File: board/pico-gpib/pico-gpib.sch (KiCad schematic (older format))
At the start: 37 parts, among them J2 USB_B_Micro, J3 RasPi_Header_40W, J4 Debug, U1 RP2040, U4 W25Q128JVS, U5 NCP1117-3.3, U6 CAT24C32, Y1 12M10PI/XT324-10/20

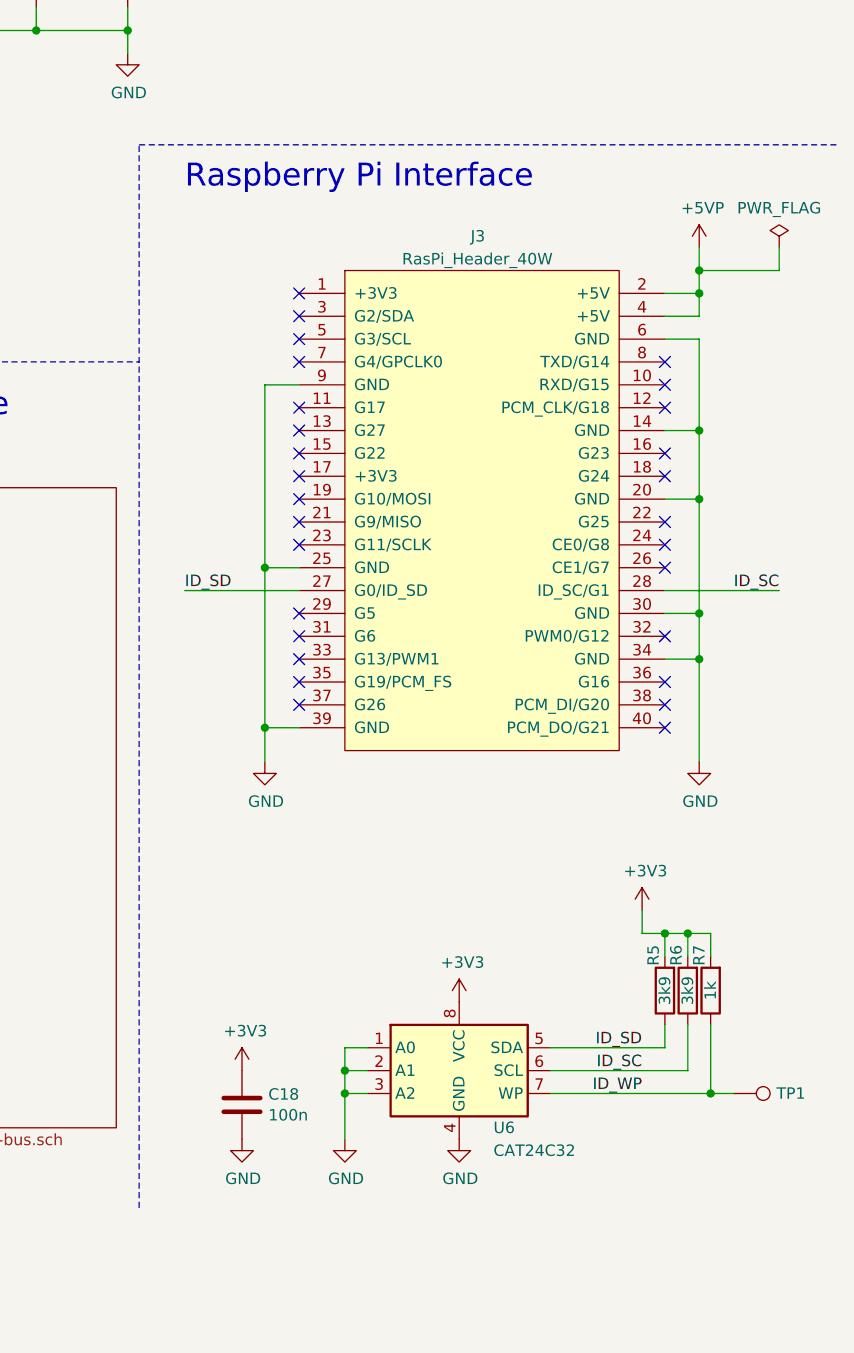
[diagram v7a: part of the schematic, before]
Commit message: Move ID EEPROM to RPI 3V3 supply.
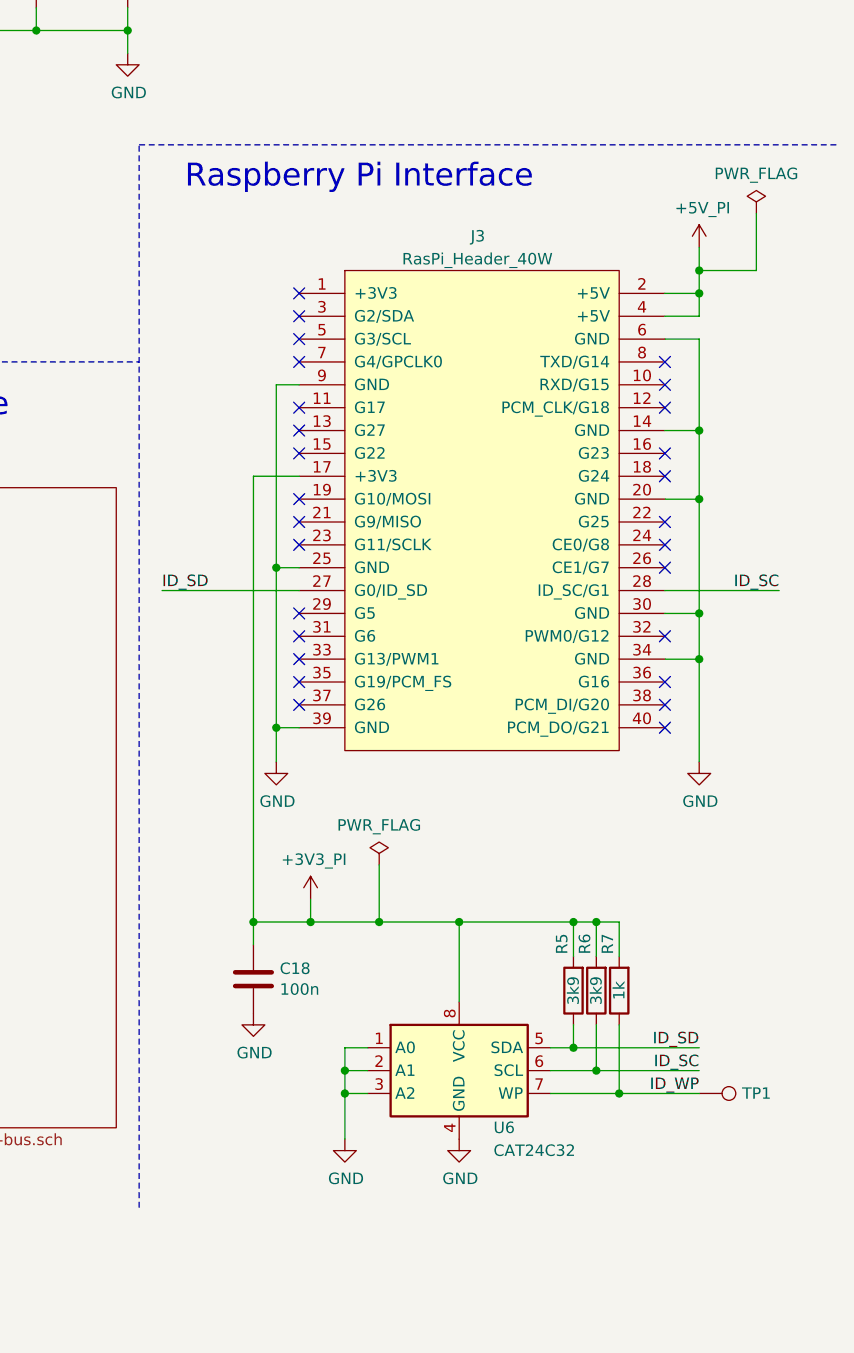
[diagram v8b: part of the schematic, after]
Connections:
- net +3V3: no longer C18.1, R5.2, R6.2, R7.2, U6.8 (VCC)
- net +3V3_PI: now reaches J3.17 (+3V3)
- net +3V3_PI: now also C18.1, R5.2, R6.2, R7.2, U6.8 (VCC)
- net +5VP renamed +5V_PI
- no-connect marks 40 -> 39
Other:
- moved on the sheet: C18, R5, R6, R7, TP1
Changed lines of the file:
@@
-$EndComp
-$Comp
-L power:+3V3 #PWR013
-U 1 1 63111360
-P 9550 5600
-F 0 "#PWR013" H 9550 5450 50  0001 C CNN
-F 1 "+3V3" H 9565 5773 50  0000 C CNN
-F 2 "" H 9550 5600 50  0001 C CNN
-F 3 "" H 9550 5600 50  0001 C CNN
-	1    9550 5600
-	1    0    0    -1
 $EndComp
 $Comp
@@
 Wire Wire Line
 	9050 6000 9050 6200
-Text Label 10350 5800 2    50   ~ 0
+Text Label 10600 5800 2    50   ~ 0
 ID_SD
-Text Label 10350 5900 2    50   ~ 0
+Text Label 10600 5900 2    50   ~ 0
 ID_SC
-Text Label 10350 6000 2    50   ~ 0
+Text Label 10600 6000 2    50   ~ 0
 ID_WP
 $Comp
 L Device:R R5
 U 1 1 63178FFC
-P 10450 5550
-F 0 "R5" V 10500 5350 50  0000 L CNN
-F 1 "3k9" V 10450 5550 50  0000 C CNN
-F 2 "Resistor_SMD:R_0402_1005Metric" V 10380 5550 50  0001 C CNN
-F 3 "~" H 10450 5550 50  0001 C CNN
-	1    10450 5550
+P 10050 5550
+F 0 "R5" V 10100 5300 50  0000 L CNN
+F 1 "3k9" V 10050 5550 50  0000 C CNN
+F 2 "Resistor_SMD:R_0402_1005Metric" V 9980 5550 50  0001 C CNN
+F 3 "~" H 10050 5550 50  0001 C CNN
+	1    10050 5550
 	-1   0    0    1
 $EndComp
@@
 L Device:R R6
 U 1 1 6317A37B
-P 10550 5550
-F 0 "R6" V 10600 5350 50  0000 L CNN
-F 1 "3k9" V 10550 5550 50  0000 C CNN
-F 2 "Resistor_SMD:R_0402_1005Metric" V 10480 5550 50  0001 C CNN
-F 3 "~" H 10550 5550 50  0001 C CNN
-	1    10550 5550
+P 10150 5550
+F 0 "R6" V 10200 5300 50  0000 L CNN
+F 1 "3k9" V 10150 5550 50  0000 C CNN
+F 2 "Resistor_SMD:R_0402_1005Metric" V 10080 5550 50  0001 C CNN
+F 3 "~" H 10150 5550 50  0001 C CNN
+	1    10150 5550
 	-1   0    0    1
 $EndComp
@@
 L Device:R R7
 U 1 1 6317ACAC
-P 10650 5550
-F 0 "R7" V 10700 5350 50  0000 L CNN
-F 1 "1k" V 10650 5550 50  0000 C CNN
-F 2 "Resistor_SMD:R_0402_1005Metric" V 10580 5550 50  0001 C CNN
-F 3 "~" H 10650 5550 50  0001 C CNN
-	1    10650 5550
+P 10250 5550
+F 0 "R7" V 10300 5300 50  0000 L CNN
+F 1 "1k" V 10250 5550 50  0000 C CNN
+F 2 "Resistor_SMD:R_0402_1005Metric" V 10180 5550 50  0001 C CNN
+F 3 "~" H 10250 5550 50  0001 C CNN
+	1    10250 5550
 	-1   0    0    1
 $EndComp
 Wire Wire Line
-	10450 5800 10450 5700
-Wire Wire Line
-	9950 5800 10450 5800
-Wire Wire Line
-	10550 5900 10550 5700
-Wire Wire Line
-	9950 5900 10550 5900
-Wire Wire Line
-	10650 6000 10650 5700
-Wire Wire Line
-	9950 6000 10650 6000
-Wire Wire Line
-	10650 6000 10750 6000
-Connection ~ 10650 6000
+	10050 5800 10050 5700
+Wire Wire Line
+	9950 5800 10050 5800
+Wire Wire Line
+	10150 5900 10150 5700
+Wire Wire Line
+	9950 5900 10150 5900
+Wire Wire Line
+	10250 6000 10250 5700
+Wire Wire Line
+	9950 6000 10250 6000
 $Comp
 L Connector:TestPoint TP1
 U 1 1 631B8D19
-P 10750 6000
-F 0 "TP1" V 10750 6188 50  0000 L CNN
-F 1 "TestPoint" V 10795 6188 50  0001 L CNN
-F 2 "TestPoint:TestPoint_Pad_D1.0mm" H 10950 6000 50  0001 C CNN
-F 3 "~" H 10950 6000 50  0001 C CNN
-	1    10750 6000
+P 10600 6000
+F 0 "TP1" V 10600 6188 50  0000 L CNN
+F 1 "TestPoint" V 10645 6188 50  0001 L CNN
+F 2 "TestPoint:TestPoint_Pad_D1.0mm" H 10800 6000 50  0001 C CNN
+F 3 "~" H 10800 6000 50  0001 C CNN
+	1    10600 6000
 	0    1    1    0
 $EndComp
-$Comp
-L power:+3V3 #PWR015
-U 1 1 631B93BC
-P 10350 5200
-F 0 "#PWR015" H 10350 5050 50  0001 C CNN
-F 1 "+3V3" H 10365 5373 50  0000 C CNN
-F 2 "" H 10350 5200 50  0001 C CNN
-F 3 "" H 10350 5200 50  0001 C CNN
-	1    10350 5200
-	1    0    0    -1
-$EndComp
-Wire Wire Line
-	10350 5200 10350 5300
-Wire Wire Line
-	10350 5300 10450 5300
-Wire Wire Line
-	10650 5300 10650 5400
-Wire Wire Line
-	10550 5400 10550 5300
-Connection ~ 10550 5300
-Wire Wire Line
-	10550 5300 10650 5300
-Wire Wire Line
-	10450 5400 10450 5300
-Connection ~ 10450 5300
-Wire Wire Line
-	10450 5300 10550 5300
+Wire Wire Line
+	10250 5250 10250 5400
+Wire Wire Line
+	10150 5400 10150 5250
+Connection ~ 10150 5250
+Wire Wire Line
+	10150 5250 10250 5250
+Wire Wire Line
+	10050 5400 10050 5250
+Connection ~ 10050 5250
+Wire Wire Line
+	10050 5250 10150 5250
 NoConn ~ 8850 2600
 NoConn ~ 8850 2700
@@
 NoConn ~ 8850 3100
 NoConn ~ 8850 3200
-NoConn ~ 8850 3300
 NoConn ~ 8850 3400
 NoConn ~ 8850 3500
@@
 L power:GND #PWR017
 U 1 1 63499121
-P 8600 6200
-F 0 "#PWR017" H 8600 5950 50  0001 C CNN
-F 1 "GND" H 8605 6027 50  0000 C CNN
-F 2 "" H 8600 6200 50  0001 C CNN
-F 3 "" H 8600 6200 50  0001 C CNN
-	1    8600 6200
-	1    0    0    -1
-$EndComp
-$Comp
-L power:+3V3 #PWR016
-U 1 1 634996AF
-P 8600 5900
-F 0 "#PWR016" H 8600 5750 50  0001 C CNN
-F 1 "+3V3" H 8615 6073 50  0000 C CNN
-F 2 "" H 8600 5900 50  0001 C CNN
-F 3 "" H 8600 5900 50  0001 C CNN
-	1    8600 5900
+P 8650 5650
+F 0 "#PWR017" H 8650 5400 50  0001 C CNN
+F 1 "GND" H 8655 5477 50  0000 C CNN
+F 2 "" H 8650 5650 50  0001 C CNN
+F 3 "" H 8650 5650 50  0001 C CNN
+	1    8650 5650
 	1    0    0    -1
 $EndComp
@@
 L Device:C C18
 U 1 1 634996B9
-P 8600 6050
-F 0 "C18" H 8715 6096 50  0000 L CNN
-F 1 "100n" H 8715 6005 50  0000 L CNN
-F 2 "Capacitor_SMD:C_0402_1005Metric" H 8638 5900 50  0001 C CNN
-F 3 "~" H 8600 6050 50  0001 C CNN
-	1    8600 6050
+P 8650 5500
+F 0 "C18" H 8765 5546 50  0000 L CNN
+F 1 "100n" H 8765 5455 50  0000 L CNN
+F 2 "Capacitor_SMD:C_0402_1005Metric" H 8688 5350 50  0001 C CNN
+F 3 "~" H 8650 5500 50  0001 C CNN
+	1    8650 5500
 	1    0    0    -1
 $EndComp
@@
 Connection ~ 10600 3400
 Wire Wire Line
-	8850 2900 8700 2900
+	8850 2900 8750 2900
 NoConn ~ 10450 4400
 NoConn ~ 10450 4300
@@
 Text Label 10950 3800 2    50   ~ 0
 ID_SC
-Text Label 8350 3800 0    50   ~ 0
+Text Label 8250 3800 0    50   ~ 0
 ID_SD
 Wire Wire Line
 	10450 3800 10950 3800
 Wire Wire Line
-	8850 3800 8350 3800
+	8850 3800 8250 3800
 $Comp
 L power:GND #PWR0108
 U 1 1 61F681DC
-P 8700 4550
-F 0 "#PWR0108" H 8700 4300 50  0001 C CNN
-F 1 "GND" H 8705 4377 50  0000 C CNN
-F 2 "" H 8700 4550 50  0001 C CNN
-F 3 "" H 8700 4550 50  0001 C CNN
-	1    8700 4550
+P 8750 4550
+F 0 "#PWR0108" H 8750 4300 50  0001 C CNN
+F 1 "GND" H 8755 4377 50  0000 C CNN
+F 2 "" H 8750 4550 50  0001 C CNN
+F 3 "" H 8750 4550 50  0001 C CNN
+	1    8750 4550
 	1    0    0    -1
 $EndComp
@@
 $EndComp
 Wire Wire Line
-	8700 4400 8700 4550
-Connection ~ 8700 4400
-Wire Wire Line
-	8850 4400 8700 4400
-Wire Wire Line
-	8700 3700 8700 4400
-Connection ~ 8700 3700
-Wire Wire Line
-	8850 3700 8700 3700
-Wire Wire Line
-	8700 2900 8700 3700
+	8750 4400 8750 4550
+Connection ~ 8750 4400
+Wire Wire Line
+	8850 4400 8750 4400
+Wire Wire Line
+	8750 3700 8750 4400
+Connection ~ 8750 3700
+Wire Wire Line
+	8850 3700 8750 3700
+Wire Wire Line
+	8750 2900 8750 3700
 Wire Wire Line
 	10600 4100 10600 4550
@@
 Wire Notes Line
 	8150 1850 11200 1850
-$Comp
-L power:+5VP #PWR0131
-U 1 1 620A68D2
+Connection ~ 10600 2500
+$Comp
+L power:PWR_FLAG #FLG0103
+U 1 1 626F016E
+P 10850 2150
+F 0 "#FLG0103" H 10850 2225 50  0001 C CNN
+F 1 "PWR_FLAG" H 10850 2323 50  0000 C CNN
+F 2 "" H 10850 2150 50  0001 C CNN
+F 3 "~" H 10850 2150 50  0001 C CNN
+	1    10850 2150
+	1    0    0    -1
+$EndComp
+Connection ~ 10050 5800
+Connection ~ 10150 5900
+Wire Wire Line
+	10050 5800 10600 5800
+Wire Wire Line
+	10150 5900 10600 5900
+Wire Wire Line
+	10250 6000 10600 6000
+Connection ~ 10250 6000
+Wire Wire Line
+	8850 3300 8650 3300
+Wire Wire Line
+	8650 3300 8650 5250
+Wire Wire Line
+	8650 5250 8900 5250
+Wire Wire Line
+	8650 5350 8650 5250
+Connection ~ 8650 5250
+Wire Wire Line
+	9550 5600 9550 5250
+Connection ~ 9550 5250
+Wire Wire Line
+	9550 5250 10050 5250
+$Comp
+L local:+5V_PI #PWR0131
+U 1 1 6281E388
 P 10600 2300
 F 0 "#PWR0131" H 10600 2150 50  0001 C CNN
-F 1 "+5VP" H 10615 2473 50  0000 C CNN
+F 1 "+5V_PI" H 10615 2473 50  0000 C CNN
 F 2 "" H 10600 2300 50  0001 C CNN
 F 3 "" H 10600 2300 50  0001 C CNN
@@
 	1    0    0    -1
 $EndComp
-Connection ~ 10600 2500
 Wire Wire Line
 	10600 2300 10600 2400
-$Comp
-L power:PWR_FLAG #FLG0103
-U 1 1 626F016E
-P 10950 2300
-F 0 "#FLG0103" H 10950 2375 50  0001 C CNN
-F 1 "PWR_FLAG" H 10950 2473 50  0000 C CNN
-F 2 "" H 10950 2300 50  0001 C CNN
-F 3 "~" H 10950 2300 50  0001 C CNN
-	1    10950 2300
-	1    0    0    -1
-$EndComp
-Wire Wire Line
-	10950 2300 10950 2400
-Wire Wire Line
-	10950 2400 10600 2400
+Wire Wire Line
+	10600 2400 10850 2400
+Wire Wire Line
+	10850 2400 10850 2150
 Connection ~ 10600 2400
 Wire Wire Line
 	10600 2400 10600 2500
+$Comp
+L local:+3V3_PI #PWR0132
+U 1 1 62830914
+P 8900 5150
+F 0 "#PWR0132" H 8900 5000 50  0001 C CNN
+F 1 "+3V3_PI" H 8915 5323 50  0000 C CNN
+F 2 "" H 8900 5150 50  0001 C CNN
+F 3 "" H 8900 5150 50  0001 C CNN
+	1    8900 5150
+	1    0    0    -1
+$EndComp
+$Comp
+L power:PWR_FLAG #FLG0104
+U 1 1 628316F1
+P 9200 5000
+F 0 "#FLG0104" H 9200 5075 50  0001 C CNN
+F 1 "PWR_FLAG" H 9200 5173 50  0000 C CNN
+F 2 "" H 9200 5000 50  0001 C CNN
+F 3 "~" H 9200 5000 50  0001 C CNN
+	1    9200 5000
+	1    0    0    -1
+$EndComp
+Wire Wire Line
+	8900 5150 8900 5250
+Connection ~ 8900 5250
+Wire Wire Line
+	8900 5250 9200 5250
+Wire Wire Line
+	9200 5250 9200 5000
+Connection ~ 9200 5250
+Wire Wire Line
+	9200 5250 9550 5250
 $EndSCHEMATC
